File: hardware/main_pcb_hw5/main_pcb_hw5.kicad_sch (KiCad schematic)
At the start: 17 parts, among them J1 Barrel_Jack(+12V), J2 5V Buck (MPM3610), J3 3.3V Buck (MPM3610), J4 CART SLOT TOP ROW, J5 CART SLOT BOTTOM ROW, J6 Conn_01x07, J7 EXP1, J8 EXP2, SW1 POWER

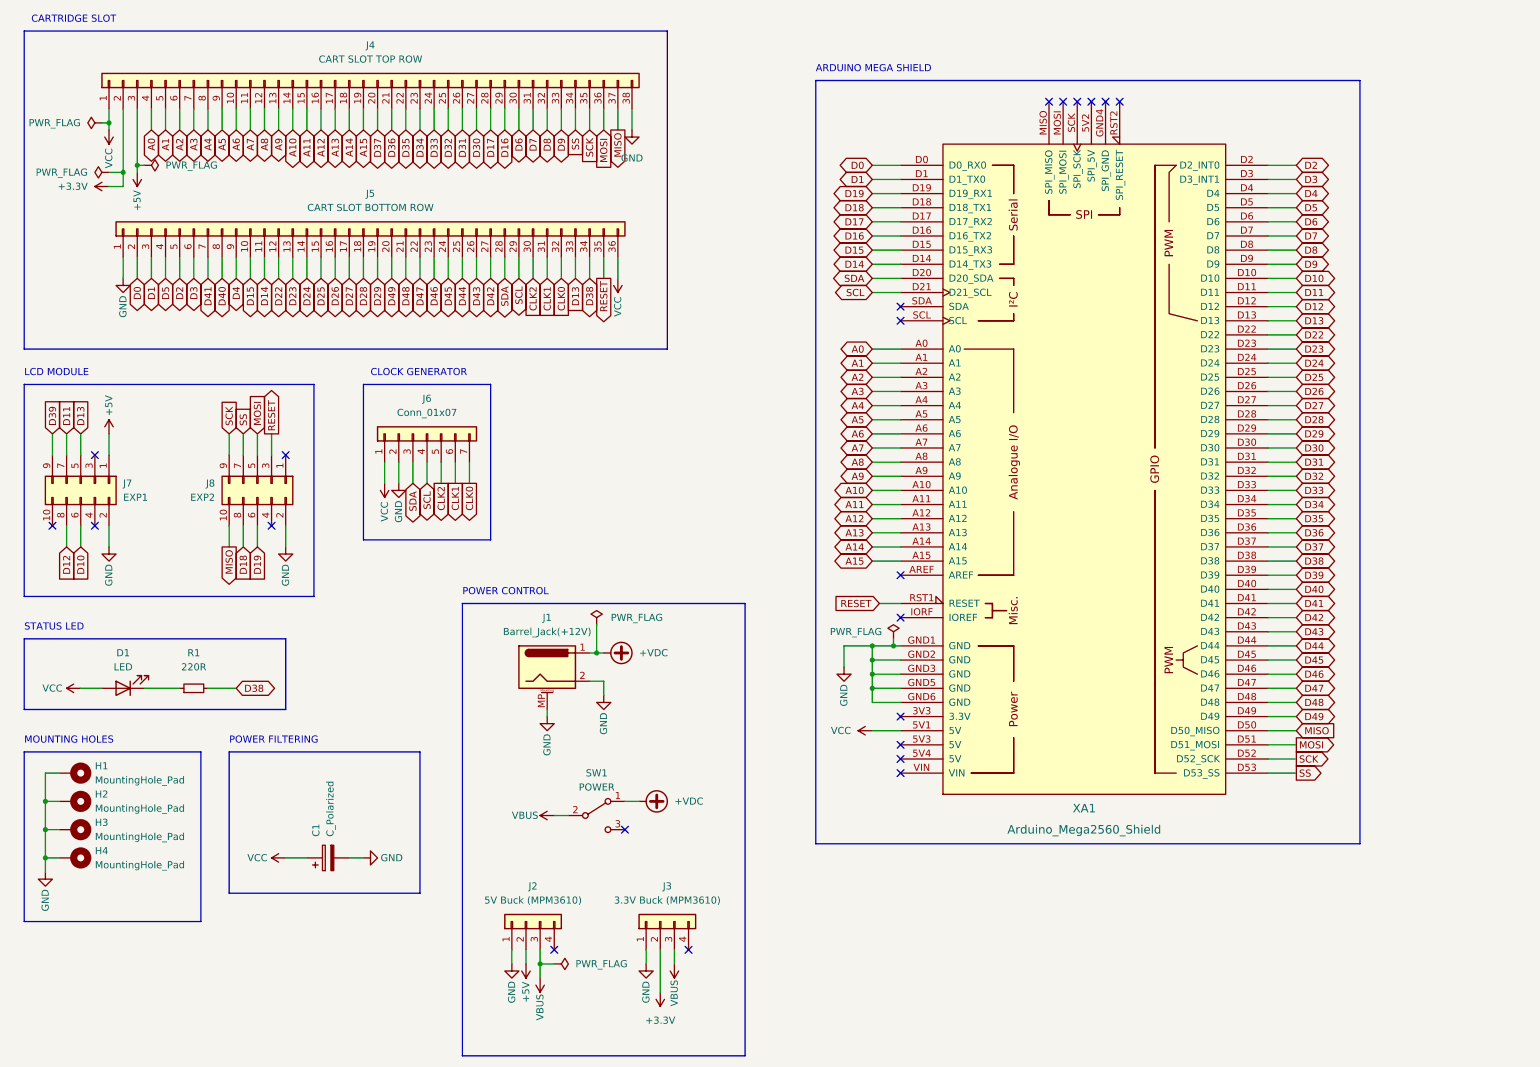
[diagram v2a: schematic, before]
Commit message: Move main PCB updates to clean branch
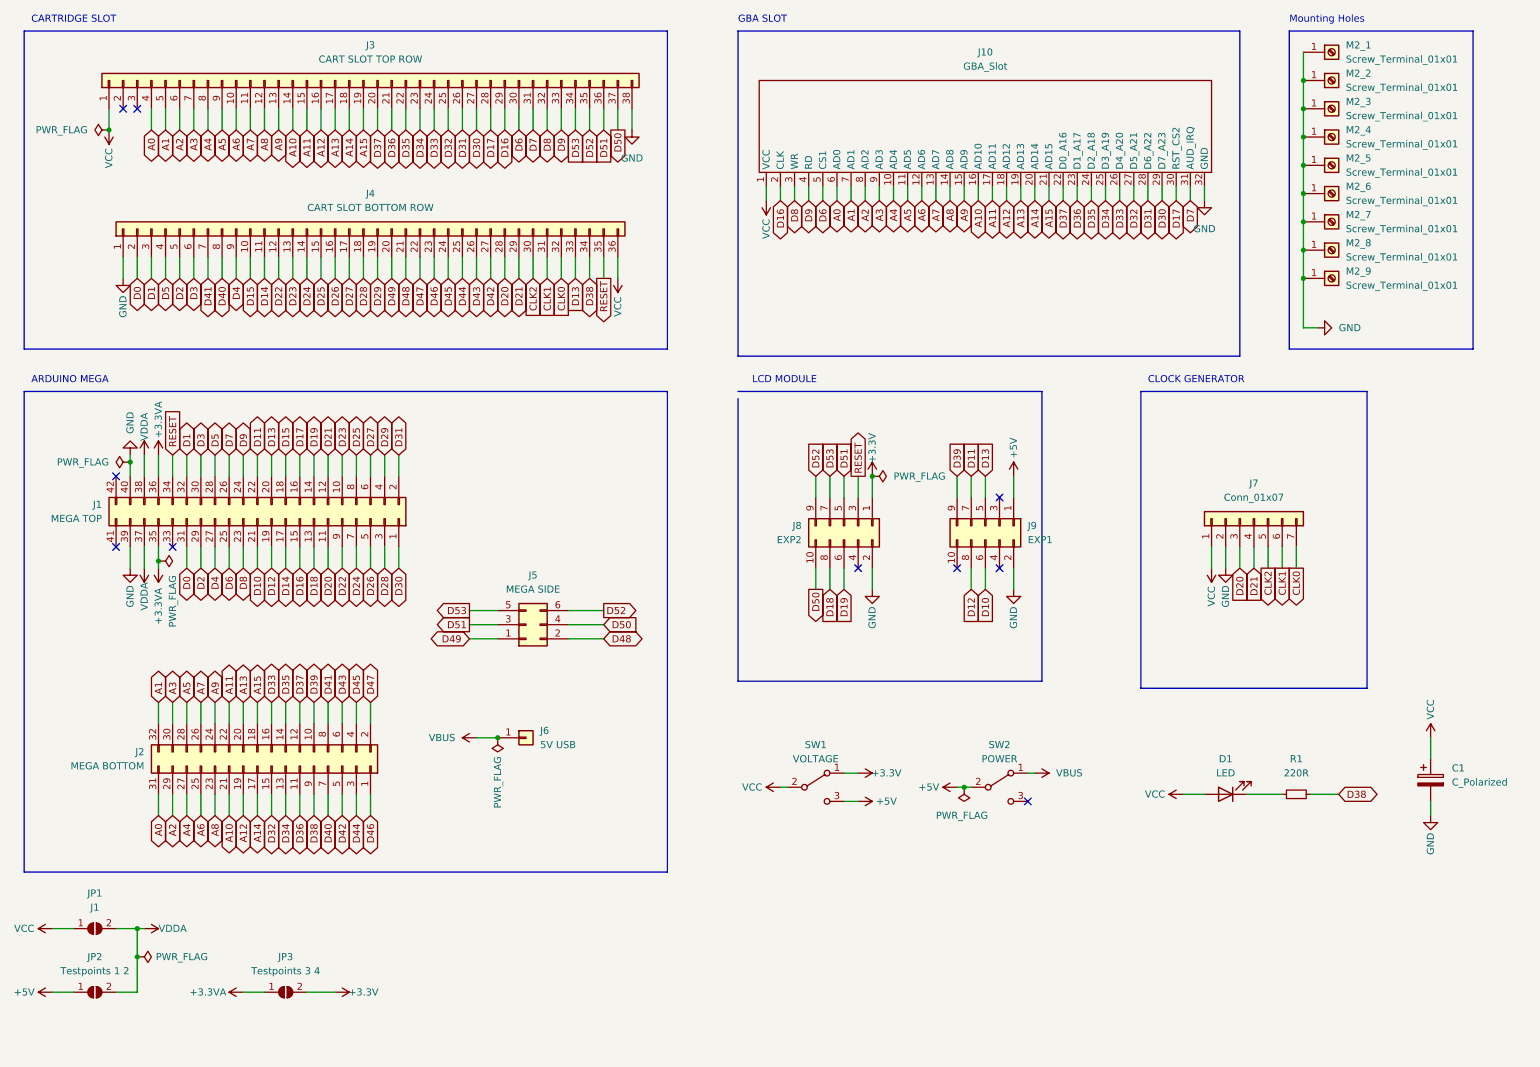
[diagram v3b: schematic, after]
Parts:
- removed H1, H2, H3, H4: MountingHole_Pad, MountingHole:MountingHole_3.2mm_M3_Pad, symbol Mechanical:MountingHole_Pad
- removed J1: Barrel_Jack(+12V), Connector_BarrelJack:BarrelJack_Horizontal, symbol Connector:Barrel_Jack_MountingPin
- removed J2: 5V Buck (MPM3610), Connector_PinHeader_2.54mm:PinHeader_1x04_P2.54mm_Vertical, symbol Connector_Generic:Conn_01x04
- removed J3: 3.3V Buck (MPM3610), Connector_PinHeader_2.54mm:PinHeader_1x04_P2.54mm_Vertical, symbol Connector_Generic:Conn_01x04
- removed XA1: Arduino_Mega2560_Shield, Arduino_Library:Arduino_Mega2560_Shield, symbol arduino_boards_library:Arduino_Mega2560_Shield
- added J1: MEGA TOP, Connector_PinSocket_2.54mm:PinSocket_2x21_P2.54mm_Vertical, symbol Connector_Generic:Conn_02x21_Odd_Even
- added J10: GBA_Slot, !OSCR:GBA_Slot, symbol !OSCR:GBA_Slot
- added J2: MEGA BOTTOM, Connector_PinSocket_2.54mm:PinSocket_2x16_P2.54mm_Vertical, symbol Connector_Generic:Conn_02x16_Odd_Even
- added J5: MEGA SIDE, Connector_PinSocket_2.54mm:PinSocket_2x03_P2.54mm_Vertical, symbol Connector_Generic:Conn_02x03_Odd_Even
- added J6: 5V USB, Connector_PinHeader_2.54mm:PinHeader_1x01_P2.54mm_Vertical, symbol Connector_Generic:Conn_01x01
- added JP1: J1, Jumper:SolderJumper-2_P1.3mm_Open_Pad1.0x1.5mm, symbol Jumper:SolderJumper_2_Open
- added JP2: Testpoints 1 2, Jumper:SolderJumper-2_P1.3mm_Open_Pad1.0x1.5mm, symbol Jumper:SolderJumper_2_Open
- added JP3: Testpoints 3 4, Jumper:SolderJumper-2_P1.3mm_Open_Pad1.0x1.5mm, symbol Jumper:SolderJumper_2_Open
- added M2_1, M2_2, M2_3, M2_4, M2_5, M2_6, M2_7, M2_8, M2_9: Screw_Terminal_01x01, MountingHole:MountingHole_2.2mm_M2_ISO7380_Pad, symbol Connector:Screw_Terminal_01x01
- added SW1: VOLTAGE, Button_Switch_THT:SW_CuK_OS102011MA1QN1_SPDT_Angled, symbol Switch:SW_SPDT
- renumbered J4 to J3, J5 to J4, J6 to J7, J7 to J9, SW1 to SW2
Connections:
- net +VDC is gone; now on net VBUS: SW2.1 (A)
- net +5V: now also SW2.2 (B), JP2.1 (A), SW1.3 (C); no longer J3.3 (Pin_3)
- net A0: now also J10.6 (AD0), J2.31 (Pin_31)
- net A1: now also J10.7 (AD1), J2.32 (Pin_32)
- net A10: now also J10.16 (AD10), J2.21 (Pin_21)
- net A11: now also J10.17 (AD11), J2.22 (Pin_22)
- net A12: now also J10.18 (AD12), J2.19 (Pin_19)
- net A13: now also J10.19 (AD13), J2.20 (Pin_20)
- net A14: now also J10.20 (AD14), J2.17 (Pin_17)
- net A15: now also J10.21 (AD15), J2.18 (Pin_18)
- net A2: now also J10.8 (AD2), J2.29 (Pin_29)
- net A3: now also J10.9 (AD3), J2.30 (Pin_30)
- net A4: now also J10.10 (AD4), J2.27 (Pin_27)
- net A5: now also J10.11 (AD5), J2.28 (Pin_28)
- net A6: now also J10.12 (AD6), J2.25 (Pin_25)
- net A7: now also J10.13 (AD7), J2.26 (Pin_26)
- net A8: now also J10.14 (AD8), J2.23 (Pin_23)
- net A9: now also J10.15 (AD9), J2.24 (Pin_24)
- net D0: now also J1.31 (Pin_31)
- net D1: now also J1.32 (Pin_32)
- net D10: now also J1.21 (Pin_21)
- net D11: now also J1.22 (Pin_22)
- net D12: now also J1.19 (Pin_19)
- net D13: now also J1.20 (Pin_20)
- net D14: now also J1.17 (Pin_17)
- net D15: now also J1.18 (Pin_18)
- net D16: now also J1.15 (Pin_15), J10.2 (CLK)
- net D17: now also J1.16 (Pin_16), J10.30 (RST_CS2)
- net D18: now also J1.13 (Pin_13)
- net D19: now also J1.14 (Pin_14)
- net D2: now also J1.29 (Pin_29)
- net D22: now also J1.9 (Pin_9)
- net D23: now also J1.10 (Pin_10)
- net D24: now also J1.7 (Pin_7)
- net D25: now also J1.8 (Pin_8)
- net D26: now also J1.5 (Pin_5)
- net D27: now also J1.6 (Pin_6)
- net D28: now also J1.3 (Pin_3)
- net D29: now also J1.4 (Pin_4)
- net D3: now also J1.30 (Pin_30)
- net D30: now also J1.1 (Pin_1), J10.29 (D7_A23)
- net D31: now also J1.2 (Pin_2), J10.28 (D6_A22)
- net D32: now also J10.27 (D5_A21), J2.15 (Pin_15)
- net D33: now also J10.26 (D4_A20), J2.16 (Pin_16)
- net D34: now also J10.25 (D3_A19), J2.13 (Pin_13)
- net D35: now also J10.24 (D2_A18), J2.14 (Pin_14)
- net D36: now also J10.23 (D1_A17), J2.11 (Pin_11)
- net D37: now also J10.22 (D0_A16), J2.12 (Pin_12)
- net D38: now also J2.9 (Pin_9)
- net D39: now also J2.10 (Pin_10)
- net D4: now also J1.27 (Pin_27)
- net D40: now also J2.7 (Pin_7)
- net D41: now also J2.8 (Pin_8)
- net D42: now also J2.5 (Pin_5)
- net D43: now also J2.6 (Pin_6)
- net D44: now also J2.3 (Pin_3)
- net D45: now also J2.4 (Pin_4)
- net D46: now also J2.1 (Pin_1)
- net D47: now also J2.2 (Pin_2)
- net D48: now also J5.2 (Pin_2)
- net D49: now also J5.1 (Pin_1)
- net D5: now also J1.28 (Pin_28)
- net D6: now also J1.25 (Pin_25), J10.5 (CS1)
- net D7: now also J1.26 (Pin_26), J10.31 (AUD_IRQ)
- net D8: now also J1.23 (Pin_23), J10.3 (WR)
- net D9: now also J1.24 (Pin_24), J10.4 (RD)
- net GND: now also J1.39 (Pin_39), J1.40 (Pin_40), J10.32 (GND), M2_1.1 (Pin_1), M2_2.1 (Pin_1), M2_3.1 (Pin_1), M2_4.1 (Pin_1), M2_5.1 (Pin_1), M2_6.1 (Pin_1), M2_7.1 (Pin_1), M2_8.1 (Pin_1), M2_9.1 (Pin_1)
- net RESET: now also J1.34 (Pin_34)
- net VBUS: now also J6.1 (Pin_1); no longer SW2.2 (B)
- net VCC: now also J10.1 (VCC), JP1.1 (A), SW1.2 (B)
- net +3V3: now reaches J8.1 (Pin_1)
- net +3V3: now also JP3.2 (B), SW1.1 (A)
- net +3.3V: no longer names the net of J3.2 (Pin_2)
- net MISO renamed D50
- net D50: now also J5.4 (Pin_4)
- net MOSI renamed D51
- net D51: now also J5.3 (Pin_3)
- net SCK renamed D52
- net D52: now also J5.6 (Pin_6)
- net SCL renamed D21
- net D21: now also J1.12 (Pin_12)
- net SDA renamed D20
- net D20: now also J1.11 (Pin_11)
- net SS renamed D53
- net D53: now also J5.5 (Pin_5)
- new net +3.3VA: J1.35 (Pin_35), J1.36 (Pin_36), JP3.1 (A)
- new net VDDA: J1.37 (Pin_37), J1.38 (Pin_38), JP1.2 (B), JP2.2 (B)
- no-connect marks 22 -> 10
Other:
- note added: "ARDUINO MEGA"
- note added: "GBA SLOT"
- note added: "Mounting Holes"
- note removed: "ARDUINO MEGA SHIELD"
- note removed: "MOUNTING HOLES"
- note removed: "POWER CONTROL"
- note removed: "POWER FILTERING"
- note removed: "STATUS LED"
- title: OSCR Shield -> OSCR HW5
- moved on the sheet: C1, D1, J7, J8, J9, R1, SW2
